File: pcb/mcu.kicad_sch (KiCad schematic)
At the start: 5 parts, among them J4 20021121-00010T4LF, U6 WT02V40V

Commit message: pcb: simplify power supply and define LC filter
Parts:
- added C20: 4.7µF, Capacitor_SMD:C_0603_1608Metric, symbol Device:C_Small
- U6: value WT02V40V -> WT02V40V-V2
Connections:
- net CHG_LP: now also U6.Z6 (P115); no longer U6.A6 (P108)
- net GND: now also C20.2
- net VDDD_VSEL: now also U6.C5 (P020); no longer U6.E2 (P106)
- net USB_DBG: no longer names the net of U6.E1 (P105)
- net USB_INT: no longer names the net of U6.E0 (P104)
- net VBUS renamed VBUS_DET
- net VBUS_DET: now also C20.1
- new net CHG_EN: U6.A6 (P108)

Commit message: pcb: pretty much the final version
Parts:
- C20: manf# (none) -> CL10A475MA8NQN
- J4: manf# (none) -> 20021121-00010T4LF
- R11, R12: value TBD -> 1.21k; manf# (none) -> RC0402FR-131K21L
- U6: value WT02V40V-V2 -> WT02C40C-V3; footprint zeus-le:WT02V40V -> zeus-le:WT02C40C; manf# (none) -> WT02C40C-V3
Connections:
- net CHG_PG: now also U6.Z5 (P114); no longer U6.A4 (P016)
- no-connect marks 13 -> 14
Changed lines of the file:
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@@
+	)
+	(no_connect
+		(at 110.49 104.14)
 	)
 	(no_connect
@@
 	(wire
 		(pts
-			(xy 110.49 118.11) (xy 110.49 104.14)
-		)
-		(stroke
-			(width 0)
-			(type default)
-		)
-	)
-	(wire
-		(pts
 			(xy 224.79 59.69) (xy 245.11 59.69)
 		)
@@
 	(wire
 		(pts
+			(xy 104.14 135.89) (xy 95.25 135.89)
+		)
+		(stroke
+			(width 0)
+			(type default)
+		)
+	)
+	(wire
+		(pts
 			(xy 71.12 111.76) (xy 85.09 111.76)
 		)
@@
 		)
 	)
+	(wire
+		(pts
+			(xy 95.25 135.89) (xy 95.25 104.14)
+		)
+		(stroke
+			(width 0)
+			(type default)
+		)
+	)
 	(bus
 		(pts
@@
 		(pts
 			(xy 204.47 73.66) (xy 224.79 73.66)
-		)
-		(stroke
-			(width 0)
-			(type default)
-		)
-	)
-	(wire
-		(pts
-			(xy 118.11 118.11) (xy 110.49 118.11)
 		)
 		(stroke
@@
 	(hierarchical_label "CHG_PG"
 		(shape input)
-		(at 118.11 118.11 0)
+		(at 104.14 135.89 0)
 		(fields_autoplaced yes)
 		(effects
@@
 			)
 		)
+		(property "manf#" "CL10A475MA8NQN"
+			(at 257.81 109.22 0)
+			(effects
+				(font
+					(size 1.27 1.27)
+				)
+				(hide yes)
+			)
+		)
 		(pin "2"
 		)
@@
 			)
 		)
-		(property "Value" "TBD"
+		(property "Value" "1.21k"
 			(at 62.23 53.3399 0)
 			(effects
@@
 			)
 		)
-		(property "Description" "Resistor, small US symbol"
+		(property "Description" "Resistor, I2C pull-up"
+			(at 59.69 52.07 0)
+			(effects
+				(font
+					(size 1.27 1.27)
+				)
+				(hide yes)
+			)
+		)
+		(property "manf#" "RC0402FR-131K21L"
 			(at 59.69 52.07 0)
 			(effects
@@
 			)
 		)
-		(property "Value" "TBD"
+		(property "Value" "1.21k"
 			(at 53.34 53.3399 0)
 			(effects
@@
 			)
 		)
-		(property "Description" "Resistor, small US symbol"
+		(property "Description" "Resistor, I2C pull-up"
+			(at 50.8 52.07 0)
+			(effects
+				(font
+					(size 1.27 1.27)
+				)
+				(hide yes)
+			)
+		)
+		(property "manf#" "RC0402FR-131K21L"
 			(at 50.8 52.07 0)
 			(effects
@@
 		)
 		(property "Description" "Generic connector, double row, 02x05, odd/even pin numbering scheme (row 1 odd numbers, row 2 even numbers), script generated (kicad-library-utils/schlib/autogen/connector/)"
+			(at 252.73 59.69 0)
+			(effects
+				(font
+					(size 1.27 1.27)
+				)
+				(hide yes)
+			)
+		)
+		(property "manf#" "20021121-00010T4LF"
 			(at 252.73 59.69 0)
 			(effects
@@
 			)
 		)
-		(property "Value" "WT02V40V-V2"
+		(property "Value" "WT02C40C-V3"
 			(at 139.1535 24.13 0)
 			(effects
@@
 			)
 		)
-		(property "Footprint" "zeus-le:WT02V40V"
+		(property "Footprint" "zeus-le:WT02C40C"
 			(at 102.21 50.54 0)
 			(effects
@@
 			(effects
 				(font
+					(size 1.27 1.27)
+				)
+				(hide yes)
+			)
+		)
+		(property "manf#" "WT02C40C-V3"
+			(at 97.79 48.26 0)
+			(effects
+				(font

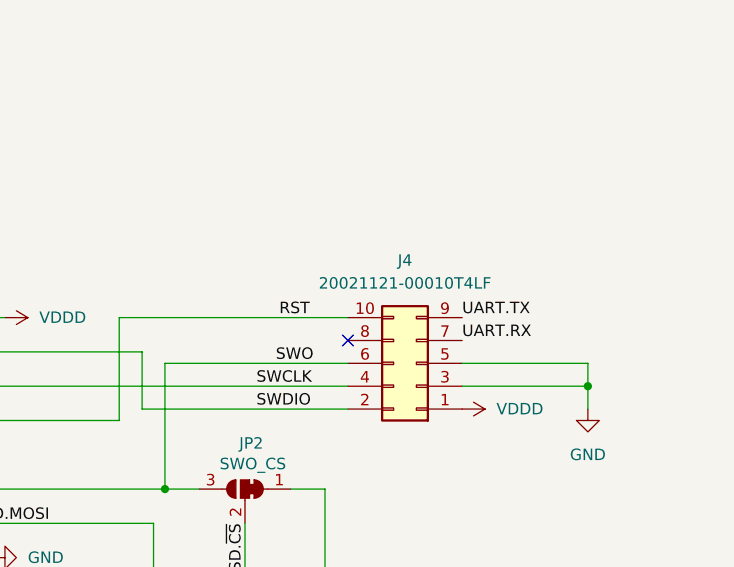
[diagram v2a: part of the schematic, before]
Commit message: pcb: use debug connector with shroud
This also gets the connector up higher so the cable won't hit the USB
connector as much.
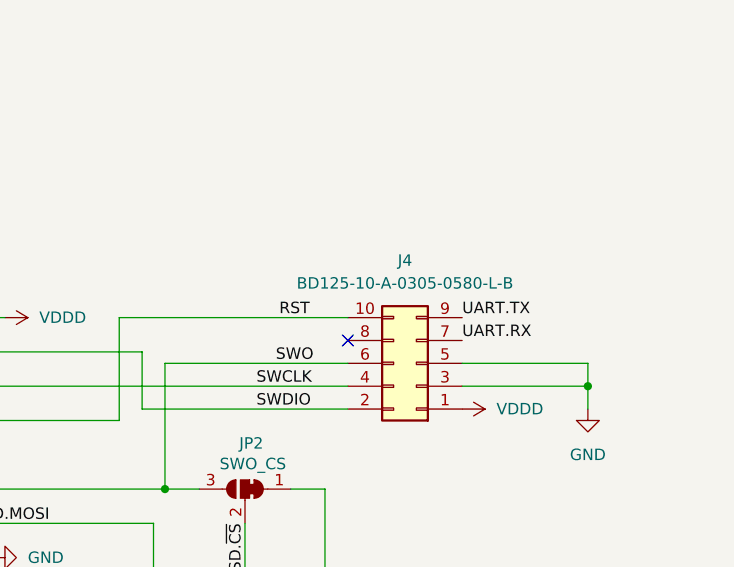
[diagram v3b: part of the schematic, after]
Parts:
- J4: value 20021121-00010T4LF -> BD125-10-A-0305-0580-L-B
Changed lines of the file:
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@@
 			)
 		)
-		(property "Value" "20021121-00010T4LF"
+		(property "Value" "BD125-10-A-0305-0580-L-B"
 			(at 251.46 50.8 0)
 			(effects
@@
 			)
 		)
-		(property "Description" "Generic connector, double row, 02x05, odd/even pin numbering scheme (row 1 odd numbers, row 2 even numbers), script generated (kicad-library-utils/schlib/autogen/connector/)"
+		(property "Description" "Connector Header Surface Mount 10 position 0.050\" (1.27mm)"
 			(at 252.73 59.69 0)
 			(effects

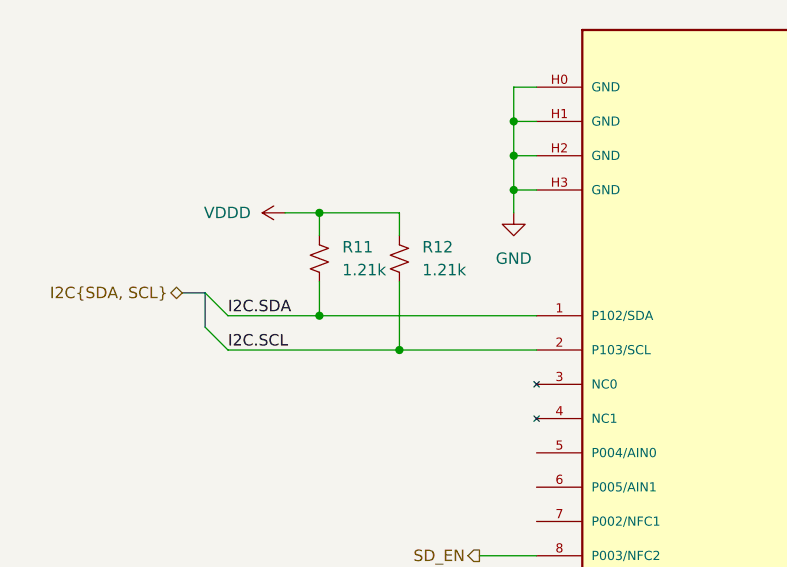
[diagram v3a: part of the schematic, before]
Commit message: pcb: rotate debug connector
This prevents it from interfering with the USB connector.
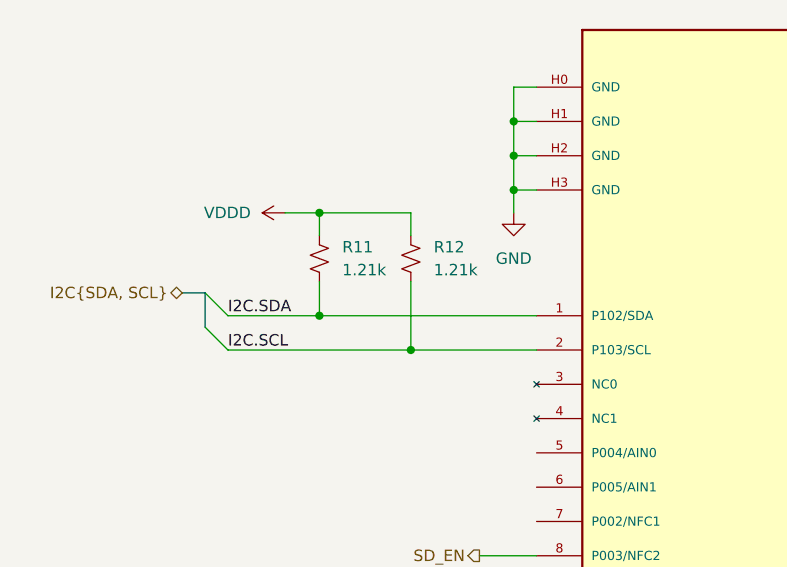
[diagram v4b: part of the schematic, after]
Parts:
- C20: manf# CL10A475MA8NQN -> C1608X5R1E475K080AC
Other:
- moved on the sheet: R12
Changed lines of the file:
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@@
 	(paper "A4")
+	(junction
+		(at 60.96 62.23)
+		(diameter 0)
+		(color 0 0 0 0)
+	)
 	(junction
 		(at 257.81 105.41)
@@
 	)
 	(junction
-		(at 59.69 62.23)
-		(diameter 0)
-		(color 0 0 0 0)
-	)
-	(junction
 		(at 72.39 44.45)
 		(diameter 0)
@@
 	(wire
 		(pts
-			(xy 59.69 46.99) (xy 50.8 46.99)
+			(xy 60.96 46.99) (xy 50.8 46.99)
 		)
 		(stroke
@@
 	(wire
 		(pts
+			(xy 60.96 62.23) (xy 74.93 62.23)
+		)
+		(stroke
+			(width 0)
+			(type default)
+		)
+	)
+	(wire
+		(pts
 			(xy 257.81 105.41) (xy 257.81 106.68)
 		)
@@
 	(wire
 		(pts
-			(xy 59.69 54.61) (xy 59.69 62.23)
+			(xy 60.96 54.61) (xy 60.96 62.23)
 		)
 		(stroke
@@
 	(wire
 		(pts
-			(xy 59.69 62.23) (xy 74.93 62.23)
-		)
-		(stroke
-			(width 0)
-			(type default)
-		)
-	)
-	(wire
-		(pts
 			(xy 220.98 125.73) (xy 220.98 115.57)
 		)
@@
 	(wire
 		(pts
-			(xy 59.69 49.53) (xy 59.69 46.99)
+			(xy 60.96 49.53) (xy 60.96 46.99)
 		)
 		(stroke
@@
 	(wire
 		(pts
-			(xy 40.64 62.23) (xy 59.69 62.23)
+			(xy 40.64 62.23) (xy 60.96 62.23)
 		)
 		(stroke
@@
 			)
 		)
-		(property "manf#" "CL10A475MA8NQN"
+		(property "manf#" "C1608X5R1E475K080AC"
 			(at 257.81 109.22 0)
 			(effects
@@
 	(symbol
 		(lib_id "Device:R_Small_US")
-		(at 59.69 52.07 0)
+		(at 60.96 52.07 0)
 		(unit 1)
 		(exclude_from_sim no)
@@
 		(fields_autoplaced yes)
 		(property "Reference" "R12"
-			(at 62.23 50.7999 0)
+			(at 63.5 50.7999 0)
 			(effects
 				(font
@@
 		)
 		(property "Value" "1.21k"
-			(at 62.23 53.3399 0)
+			(at 63.5 53.3399 0)
 			(effects
 				(font
@@
 		)
 		(property "Footprint" "Resistor_SMD:R_0402_1005Metric"
-			(at 59.69 52.07 0)
+			(at 60.96 52.07 0)
 			(effects
 				(font
@@
 		)
 		(property "Datasheet" "~"
-			(at 59.69 52.07 0)
+			(at 60.96 52.07 0)
 			(effects
 				(font
@@
 		)
 		(property "Description" "Resistor, I2C pull-up"
-			(at 59.69 52.07 0)
+			(at 60.96 52.07 0)
 			(effects
 				(font
@@
 		)
 		(property "manf#" "RC0402FR-131K21L"
-			(at 59.69 52.07 0)
-			(effects
-				(font
+			(at 60.96 52.07 0)
+			(effects
+				(font

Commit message: pcb: fix debug connector part number
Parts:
- J4: manf# 20021121-00010T4LF -> BD125-10-A-0305-0580-L-B
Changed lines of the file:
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@@
 			)
 		)
-		(property "manf#" "20021121-00010T4LF"
+		(property "manf#" "BD125-10-A-0305-0580-L-B"
 			(at 252.73 59.69 0)
 			(effects

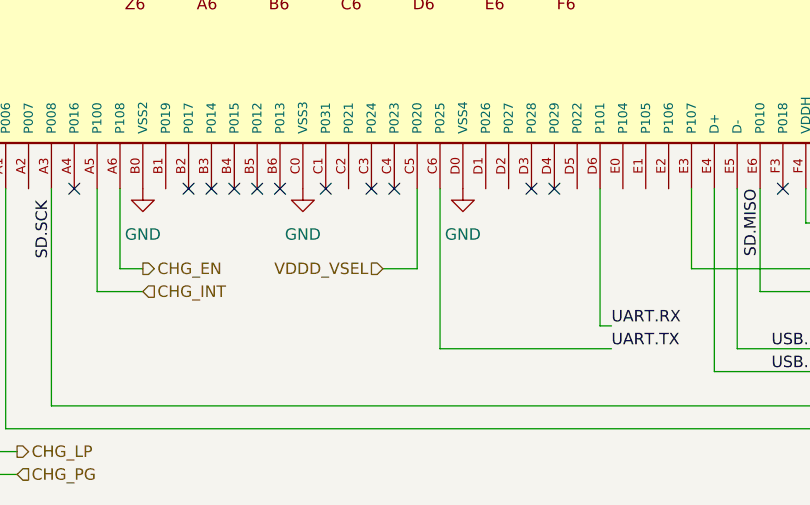
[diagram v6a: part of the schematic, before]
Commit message: pcb: add pull-downs for WiFi power
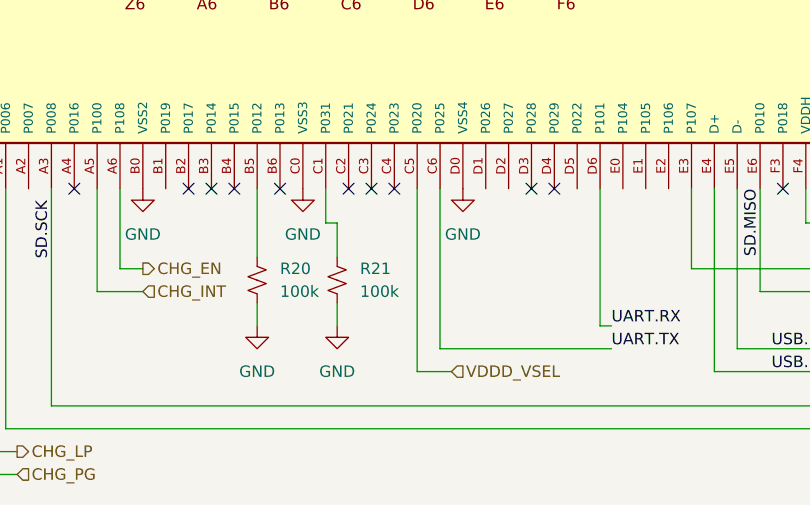
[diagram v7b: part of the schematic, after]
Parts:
- added R20, R21: 100k, Resistor_SMD:R_0402_1005Metric, symbol Device:R_Small_US
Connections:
- net GND: now also R20.2, R21.2
- net at U6.B5 (P012): now also R20.1
- net at U6.C1 (P031): now also R21.1
- no-connect marks 14 -> 13
